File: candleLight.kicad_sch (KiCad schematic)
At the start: 3 parts

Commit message: schematic
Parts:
- removed FID101, FID102, FID103: Dummy_FIDUCIAL_Passermarke_Type1_RevE_Date16Nov20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, Fiducials:Fiducial_1mm_Dia_2.54mm_Outer_CopperTop, symbol candleLight-rescue:Dummy_FIDUCIAL_Passermarke_Type1_RevE_Date16Nov2011
- added C1, C10, C2: 10uF, Capacitor_SMD:C_0805_2012Metric, symbol candleLight-rescue:C_Small
- added C11, C12, C5, C6, C7, C8, C9: 100nF, Capacitor_SMD:C_0603_1608Metric, symbol candleLight-rescue:C_Small
- added C3, C4: 20pF, Capacitor_SMD:C_0603_1608Metric, symbol candleLight-rescue:C_Small
- added D1, D2, D3: LED, LED_SMD:LED_0603_1608Metric, symbol candleLight-rescue:LED
- added J1: USB_C_Receptacle_USB2.0, stm32world:USB_C_Receptacle_HRO_TYPE-C-31-M-12, symbol stm32world:USB_C_Receptacle_USB2.0
- added R1, R2: 4K7, Resistor_SMD:R_0603_1608Metric, symbol candleLight-rescue:R
- added R10, R4, R8, R9: 1K, Resistor_SMD:R_0603_1608Metric, symbol candleLight-rescue:R
- added R11, R5: 5k1, Resistor_SMD:R_0603_1608Metric, symbol Device:R
- added R3: R, Resistor_SMD:R_0805_2012Metric, symbol candleLight-rescue:R
- added R6: 10K, Resistor_SMD:R_0603_1608Metric, symbol candleLight-rescue:R
- added R7: dnp, Resistor_SMD:R_0805_2012Metric, symbol candleLight-rescue:R
- added SCL1: SCL1, Measurement_Points:Measurement_Point_Round-SMD-Pad_Small, symbol candleLight-rescue:TEST_1P
- added SDA1: SDA1, Measurement_Points:Measurement_Point_Round-SMD-Pad_Small, symbol candleLight-rescue:TEST_1P
- added U1: ME6210A33PG, Package_TO_SOT_SMD:SOT-89-3, symbol candleLight-rescue:MCP1754ST-3302E/MB
- added U2: STM32F072C8Tx, Package_QFP:LQFP-48_7x7mm_P0.5mm, symbol MCU_ST_STM32F0:STM32F072C8Tx
- added U3: TJA1051/3, Package_SO:SOIC-8_3.9x4.9mm_P1.27mm, symbol candleLight-rescue:TJA1051/3
- added W1, W2: TEST_1P, Measurement_Points:Measurement_Point_Round-SMD-Pad_Big, symbol candleLight-rescue:TEST_1P
- added W3, W4, W5, W6, W7, W8: TEST_1P, Measurement_Points:Measurement_Point_Round-SMD-Pad_Small, symbol candleLight-rescue:TEST_1P
- added X1: CON_SWD, Connector:Tag-Connect_TC2030-IDC-NL_2x03_P1.27mm_Vertical, symbol Connector:Conn_ARM_SWD_TagConnect_TC2030-NL
- added X2: SUB-D9, Connect:DB9M_CI, symbol candleLight-rescue:SUB-D9
- added Y1: 8MHz, Crystal:Crystal_SMD_Abracon_ABM3-2Pin_5.0x3.2mm, symbol candleLight-rescue:Crystal_Small
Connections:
- new net: D1.2 (A), R8.1
- new net: R1.2, SCL1.1, U2.42 (PB6)
- new net: J1.A5 (CC1), R5.2
- new net: J1.B5 (CC2), R11.1
- new net: U2.27 (PB14), W5.1
- new net: R2.1, SDA1.1, U2.43 (PB7)
- new net: U2.25 (PB12), W3.1
- new net: R3.2, R4.2, U2.44 (BOOT0)
- new net: U2.30 (PA9), W7.1
- new net: D3.2 (A), R10.1
- new net: U2.26 (PB13), W4.1
- new net: C3.2, U2.5 (PF0), Y1.1
- new net: C4.2, U2.6 (PF1), Y1.2
- new net: U2.28 (PB15), W6.1
- new net: U2.31 (PA10), W8.1
- new net: D2.2 (A), R9.1
- new net +3V3: C10.1, C12.1, C2.1, C6.1, C7.1, C8.1, C9.1, R1.1, R10.2, R2.2, R3.1, R6.1, R8.2, R9.2, U1.3 (VO), U2.1 (VBAT), U2.24 (VDD), U2.36 (VDDIO2), U2.48 (VDD), U2.9 (VDDA), U3.5 (VIO), X1.1 (VCC)
- new net +5V: C1.1, C11.1, J1.A4 (VBUS), J1.A9 (VBUS), J1.B4 (VBUS), J1.B9 (VBUS), U1.2 (VI), U3.3 (VCC), W1.1
- new net CAN_H: R7.1, U3.7 (CAN_H), X2.7
- new net CAN_L: R7.2, U3.6 (CAN_L), X2.2
- new net CAN_RX: U2.45 (PB8), U3.4 (RXD)
- new net CAN_S: R6.2, U2.2 (PC13), U3.8 (S)
- new net CAN_TX: U2.46 (PB9), U3.1 (TXD)
- new net GND: C1.2, C10.2, C11.2, C12.2, C2.2, C3.1, C4.1, C5.2, C6.2, C7.2, C8.2, C9.2, D3.1 (K), J1.A1 (GND), J1.A12 (GND), J1.B1 (GND), J1.B12 (GND), J1.S1 (SHIELD), R11.2, R4.1, R5.1, U1.1 (GND), U2.23 (VSS), U2.35 (VSS), U2.47 (VSS), U2.8 (VSSA), U3.2 (GND), W2.1, X1.3 (GND), X2.3
- new net LED1: D1.1 (K), U2.10 (PA0)
- new net LED2: D2.1 (K), U2.11 (PA1)
- new net NRST: C5.1, U2.7 (NRST), X1.5 (~{RESET})
- new net SWCLK: U2.37 (PA14), X1.2 (SWCLK)
- new net SWDIO: U2.34 (PA13), X1.4 (SWDIO)
- new net USB_DN: J1.A7 (D-), J1.B7 (D-), U2.32 (PA11)
- new net USB_DP: J1.A6 (D+), J1.B6 (D+), U2.33 (PA12)
- no-connect marks 0 -> 28
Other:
- removed sheet CAN
- removed sheet Connectors
- removed sheet LEDs
- removed sheet MCU
- removed sheet Power
- note added: "CAN"
- note added: "Connectors"
- note added: "Leds"
- note added: "MCU"
- note added: "Power"
- title: (none) -> canleLight

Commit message: v2 ready
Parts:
- removed X1: CON_SWD, Connector:Tag-Connect_TC2030-IDC-NL_2x03_P1.27mm_Vertical, symbol Connector:Conn_ARM_SWD_TagConnect_TC2030-NL
- removed X2: SUB-D9, Connect:DB9M_CI, symbol candleLight-rescue:SUB-D9
- added J2: Conn_Phoenix, TerminalBlock_Phoenix:TerminalBlock_Phoenix_MKDS-1,5-3-5.08_1x03_P5.08mm_Horizontal, symbol Connector_Generic:Conn_01x03
- added J3: Conn_SWD, Connector_PinHeader_2.54mm:PinHeader_1x03_P2.54mm_Vertical, symbol Connector_Generic:Conn_01x03
- added J4: Conn_3.3V, Connector_PinHeader_2.54mm:PinHeader_1x02_P2.54mm_Vertical, symbol Connector_Generic:Conn_01x02
- C3, C4: MPN C91702 -> C1648
- C5: MPN C105621 -> C14663
- R11, R5: MPN (none) -> C23186
- U3: symbol candleLight-rescue:TJA1051/3 -> Interface_CAN_LIN:TJA1051T-3; MPN C51484082 -> C58988
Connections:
- net +3V3: now also J4.1 (Pin_1)
- net CAN_H: now also J2.3 (Pin_3)
- net CAN_L: now also J2.1 (Pin_1)
- net GND: now also J2.2 (Pin_2), J4.2 (Pin_2)
- net NRST: now also J3.1 (Pin_1)
- net SWCLK: now also J3.2 (Pin_2)
- net SWDIO: now also J3.3 (Pin_3)
- no-connect marks 28 -> 20
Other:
- moved on the sheet: C1, C10, C11, C12, C2, C3, C4, C5, C6, C7, C8, C9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

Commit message: production :)
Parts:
- C3, C4: value 20pF -> 30pF; MPN C1648 -> C1658
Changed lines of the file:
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@@
 			)
 		)
-		(property "Value" "20pF"
+		(property "Value" "30pF"
 			(at 65.786 51.816 90)
 			(effects
@@
 			)
 		)
-		(property "MPN" "C1648"
+		(property "MPN" "C1658"
 			(at 63.5 54.61 90)
 			(effects
@@
 		(dnp no)
 		(property "Reference" "C4"
-			(at 62.23 61.214 90)
+			(at 62.23 60.706 90)
 			(effects
 				(font
@@
 			)
 		)
-		(property "Value" "20pF"
+		(property "Value" "30pF"
 			(at 66.294 62.484 90)
 			(effects
@@
 			)
 		)
-		(property "MPN" "C1648"
+		(property "MPN" "C1658"
 			(at 63.5 59.69 90)
 			(effects

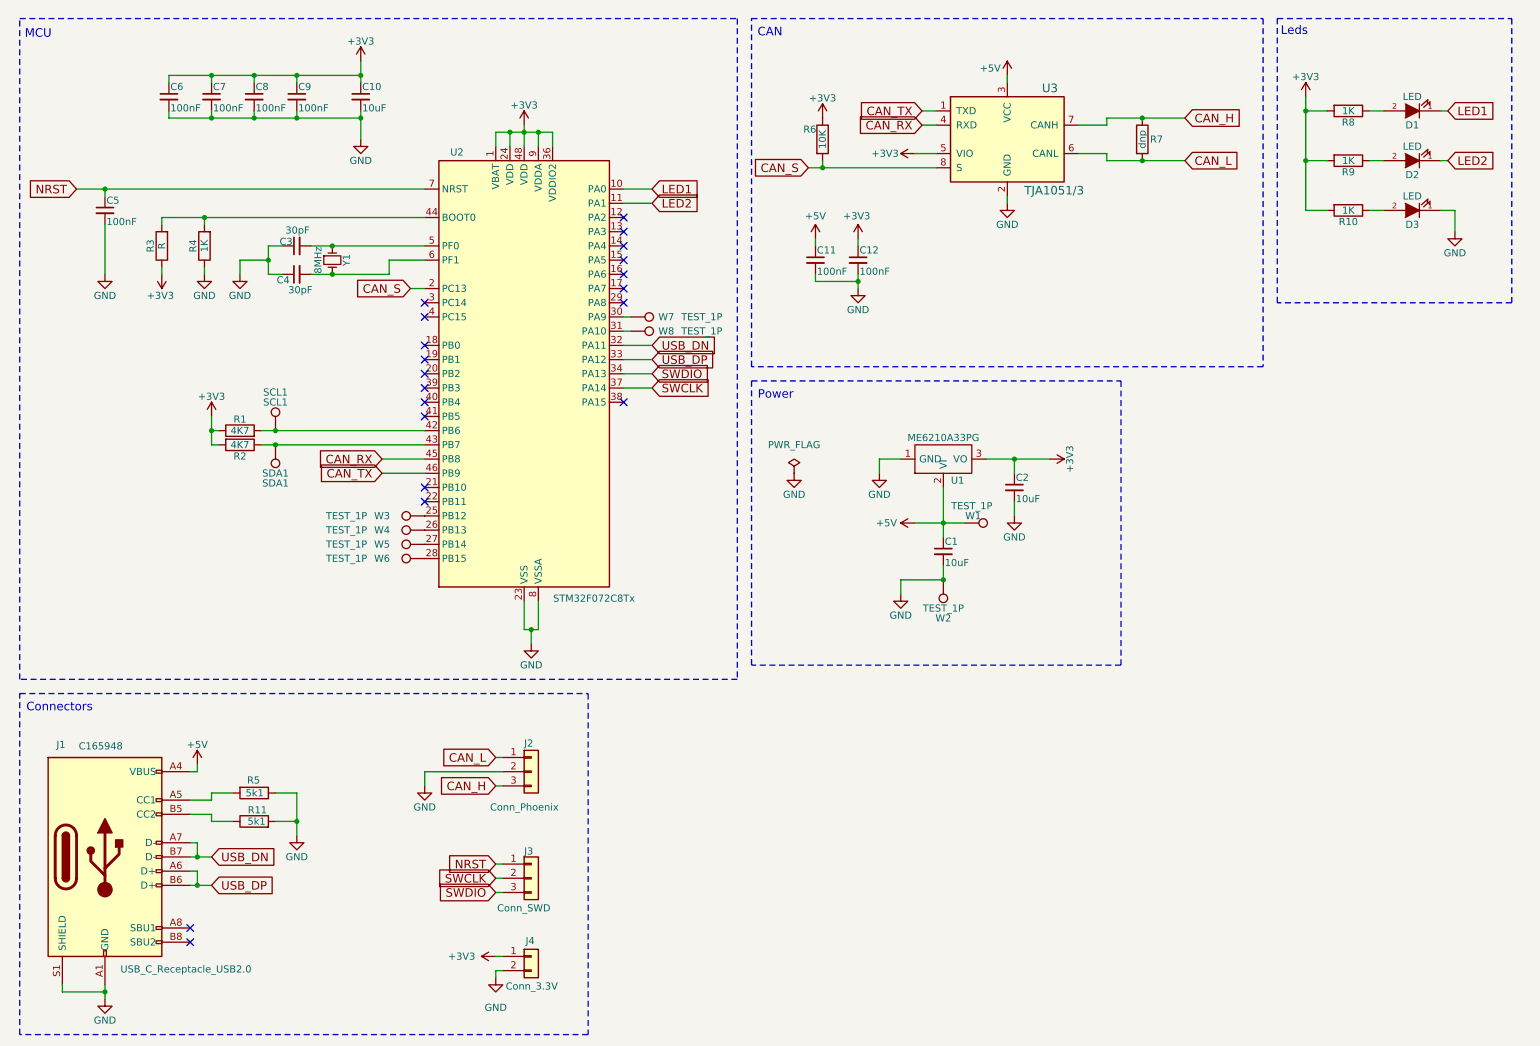
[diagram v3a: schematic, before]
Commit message: update schematic
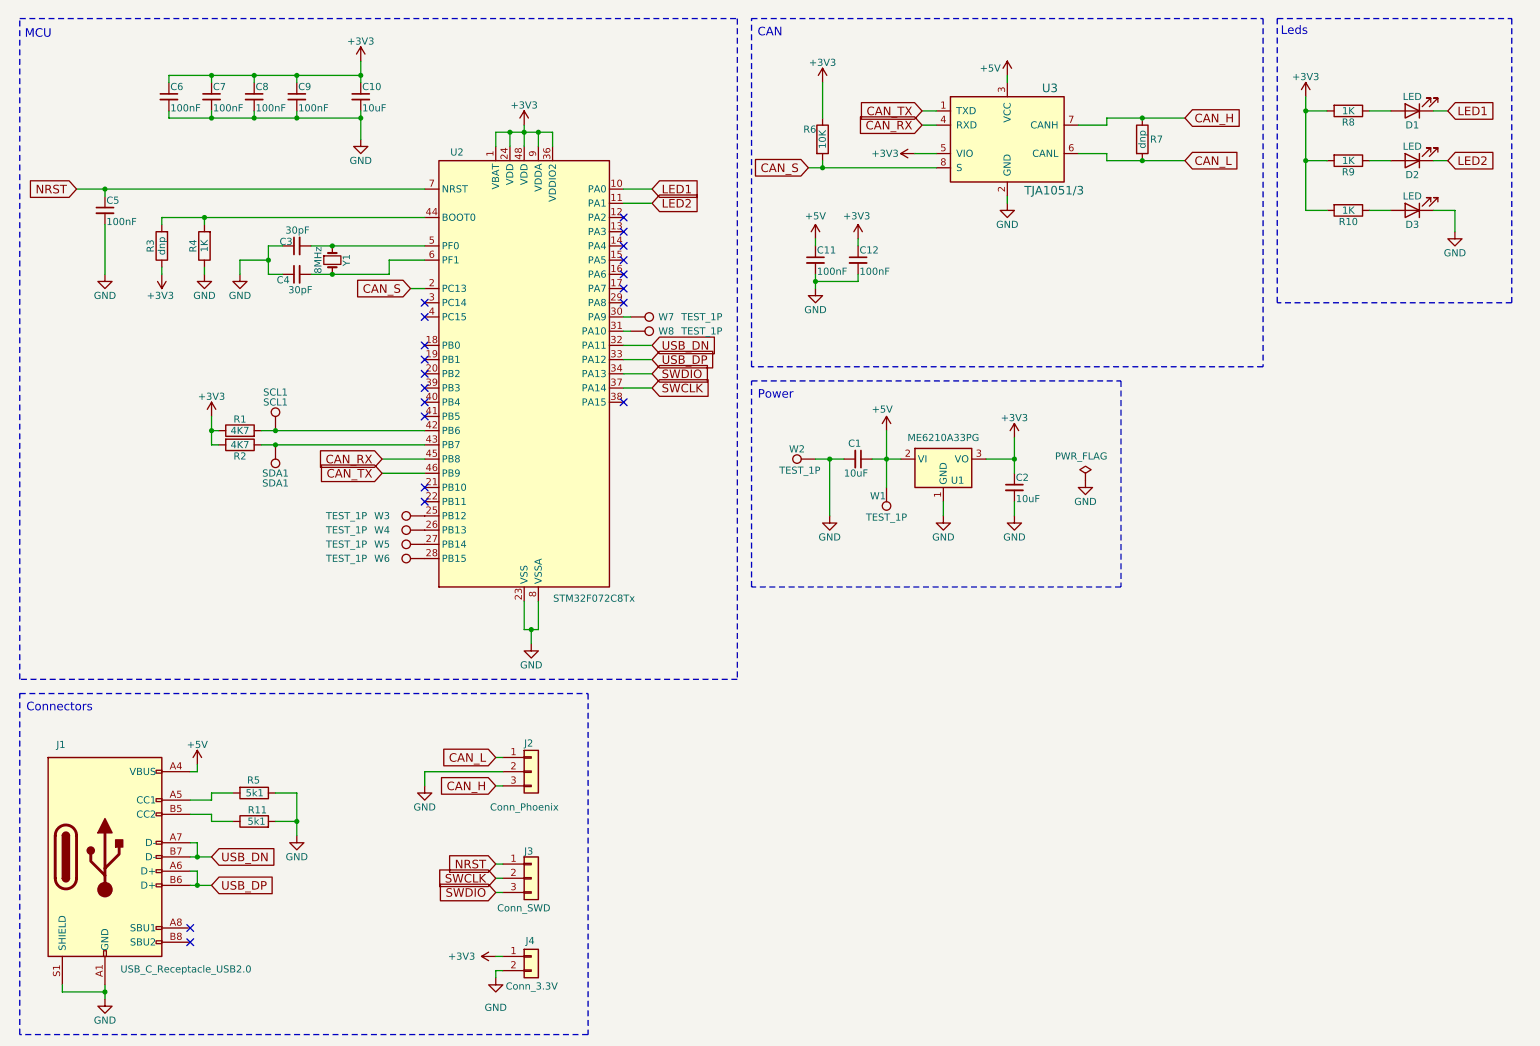
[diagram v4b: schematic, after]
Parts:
- C1, C10, C11, C12, C2, C3, C4, C5, C6, C7, C8, C9: symbol candleLight-rescue:C_Small -> Device:C_Small
- D1, D2, D3: symbol candleLight-rescue:LED -> Device:LED
- R1, R10, R2, R4, R6, R7, R8, R9: symbol candleLight-rescue:R -> Device:R
- R3: value R -> dnp; symbol candleLight-rescue:R -> Device:R
- SCL1, SDA1, W1, W2, W3, W4, W5, W6, W7, W8: symbol candleLight-rescue:TEST_1P -> Connector:TestPoint
- U1: symbol candleLight-rescue:MCP1754ST-3302E/MB -> Regulator_Linear:MCP1754S-1802xMB
- Y1: symbol candleLight-rescue:Crystal_Small -> Device:Crystal_Small
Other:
- moved on the sheet: C1, W1, W2

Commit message: LCSC
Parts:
- C1, C10, C2: LCSC (none) -> C440198; MPN C440198 -> (none)
- C11, C12, C5, C6, C7, C8, C9: LCSC (none) -> C14663; MPN C14663 -> (none)
- C3, C4: LCSC (none) -> C1658; MPN C1658 -> (none)
- D1, D2: LCSC (none) -> C2290; MPN C2290 -> (none)
- D3: LCSC (none) -> C2286; MPN C2286 -> (none)
- R1, R2: LCSC (none) -> C23162; MPN C23162 -> (none)
- R10, R4, R8, R9: LCSC (none) -> C21190; MPN C21190 -> (none)
- R11, R5: LCSC (none) -> C23186; MPN C23186 -> (none)
- R6: LCSC (none) -> C25804; MPN C25804 -> (none)
- U1: LCSC (none) -> C85233; MPN C85233 -> (none)
- U2: LCSC (none) -> C80488; MPN C80488 -> (none)
- U3: LCSC (none) -> C58988; MPN C58988 -> (none)
- Y1: LCSC (none) -> C144380; MPN C144380 -> (none)
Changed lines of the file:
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@@
 			)
 		)
-		(property "MPN" "C2290"
+		(property "LCSC" "C2290"
 			(at 262.89 30.48 0)
 			(effects
@@
 			)
 		)
-		(property "MPN" "C25804"
+		(property "LCSC" "C25804"
 			(at 157.48 35.56 90)
 			(effects
@@
 			)
 		)
-		(property "MPN" "C14663"
+		(property "LCSC" "C14663"
 			(at 55.88 27.94 0)
 			(effects
@@
 			)
 		)
-		(property "MPN" "C440198"
+		(property "LCSC" "C440198"
 			(at 191.77 97.79 0)
 			(effects
@@
 			)
 		)
-		(property "MPN" "C21190"
+		(property "LCSC" "C21190"
 			(at 251.46 30.48 90)
 			(effects
@@
 			)
 		)
-		(property "MPN" "C14663"
+		(property "LCSC" "C14663"
 			(at 48.26 27.94 0)
 			(effects
@@
 			)
 		)
-		(property "MPN" "C23162"
+		(property "LCSC" "C23162"
 			(at 53.34 90.17 90)
 			(effects
@@
 			)
 		)
-		(property "MPN" "C14663"
+		(property "LCSC" "C14663"
 			(at 163.83 57.15 0)
 			(effects
@@
 			)
 		)
-		(property "MPN" "C14663"
+		(property "LCSC" "C14663"
 			(at 156.21 57.15 0)
 			(effects
@@
 			)
 		)
-		(property "MPN" "C23186"
+		(property "LCSC" "C23186"
 			(at 55.88 157.48 90)
 			(effects
@@
 			)
 		)
-		(property "MPN" "C2286"
+		(property "LCSC" "C2286"
 			(at 262.89 48.26 0)
 			(effects
@@
 			)
 		)
-		(property "MPN" "C1658"
+		(property "LCSC" "C1658"
 			(at 63.5 54.61 90)
 			(effects
@@
 			)
 		)
-		(property "MPN" "C1658"
+		(property "LCSC" "C1658"
 			(at 63.5 59.69 90)
 			(effects
@@
 			)
 		)
-		(property "MPN" "C80488"
+		(property "LCSC" "C80488"
 			(at 104.14 77.47 0)
 			(effects
@@
 			)
 		)
-		(property "MPN" "C21190"
+		(property "LCSC" "C21190"
 			(at 46.99 54.61 90)
 			(effects
@@
 			)
 		)
-		(property "MPN" "C2290"
+		(property "LCSC" "C2290"
 			(at 262.89 39.37 0)
 			(effects
@@
 			)
 		)
-		(property "MPN" "C23186"
+		(property "LCSC" "C23186"
 			(at 55.88 152.4 90)
 			(effects
@@
 			)
 		)
-		(property "MPN" "C58988"
+		(property "LCSC" "C58988"
 			(at 190.5 35.56 0)
 			(effects
@@
 			)
 		)
-		(property "MPN" "C440198 "
+		(property "LCSC" "C440198 "
 			(at 74.93 27.94 0)
 			(effects
@@
 			)
 		)
-		(property "MPN" "C14663"
+		(property "LCSC" "C14663"
 			(at 63.5 27.94 0)
 			(effects
@@
 			)
 		)
-		(property "MPN" "C21190"
+		(property "LCSC" "C21190"
 			(at 251.46 39.37 90)
 			(effects
@@
 			)
 		)
-		(property "MPN" "C14663"
+		(property "LCSC" "C14663"
 			(at 40.64 27.94 0)
 			(effects
@@
 			)
 		)
-		(property "MPN" "C144380"
+		(property "LCSC" "C144380"
 			(at 69.85 57.15 0)
 			(effects
@@
 			)
 		)
-		(property "MPN" "C21190"
+		(property "LCSC" "C21190"
 			(at 251.46 48.26 90)
 			(effects
@@
 			)
 		)
-		(property "MPN" "C85233"
+		(property "LCSC" "C85233"
 			(at 179.07 92.71 0)
 			(effects
@@
 			)
 		)
-		(property "MPN" "C440198"
+		(property "LCSC" "C440198"
 			(at 163.83 92.71 0)
 			(effects
@@
 			)
 		)
-		(property "MPN" "C23162"
+		(property "LCSC" "C23162"
 			(at 53.34 87.63 90)
 			(effects
@@
 			)
 		)
-		(property "MPN" "C14663"
+		(property "LCSC" "C14663"
 			(at 29.21 48.26 0)
 			(effects

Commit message: inital board
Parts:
- removed C5: 100nF, Capacitor_SMD:C_0603_1608Metric, symbol Device:C_Small
- removed J3: Conn_SWD, Connector_PinHeader_2.54mm:PinHeader_1x03_P2.54mm_Vertical, symbol Connector_Generic:Conn_01x03
- removed J4: Conn_3.3V, Connector_PinHeader_2.54mm:PinHeader_1x02_P2.54mm_Vertical, symbol Connector_Generic:Conn_01x02
- removed R1, R2: 4K7, Resistor_SMD:R_0603_1608Metric, symbol Device:R
- removed R3: dnp, Resistor_SMD:R_0805_2012Metric, symbol Device:R
- removed R4: 1K, Resistor_SMD:R_0603_1608Metric, symbol Device:R
- removed SCL1: SCL1, Measurement_Points:Measurement_Point_Round-SMD-Pad_Small, symbol Connector:TestPoint
- removed SDA1: SDA1, Measurement_Points:Measurement_Point_Round-SMD-Pad_Small, symbol Connector:TestPoint
- removed W1, W2: TEST_1P, Measurement_Points:Measurement_Point_Round-SMD-Pad_Big, symbol Connector:TestPoint
- removed W3, W4, W5, W6, W7, W8: TEST_1P, Measurement_Points:Measurement_Point_Round-SMD-Pad_Small, symbol Connector:TestPoint
- added C13, C14, C3: 100nF, Capacitor_SMD:C_0603_1608Metric, symbol Device:C_Small
- added C15: 10uF, Capacitor_SMD:C_0805_2012Metric, symbol Device:C_Small
- added J3: Conn_01x05, Connector_PinHeader_2.54mm:PinHeader_1x05_P2.54mm_Vertical, symbol Connector_Generic:Conn_01x05
- added R5: 10K, Resistor_SMD:R_0603_1608Metric, symbol Device:R
- added R8: 120, Resistor_SMD:R_0603_1608Metric, symbol Device:R
- added SW1, SW2: TS-1088R-02526, stm32world:TS-1088R-02526, symbol stm32world:TS-1088R-02526
- added SW3: MST22D18G2 125, woldhack:SW-SMD_MST22D18G2, symbol woldhack:MST22D18G2125
- C1: renamed from C3; LCSC C1658 -> C1554
- C12: renamed from C10; LCSC C440198 -> C440198
- C2: renamed from C4; LCSC C1658 -> C1554
- R7: value dnp -> 10K; footprint Resistor_SMD:R_0805_2012Metric -> Resistor_SMD:R_0603_1608Metric; LCSC (none) -> C25804
- Y1: LCSC C144380 -> C115962
- renumbered C8 to C10, C9 to C11, C1 to C4, C2 to C5, C11 to C6, C6 to C7, C12 to C8, C7 to C9, R9 to R10, R10 to R11, R5 to R3, R11 to R4, R8 to R9, U2 to U1, U1 to U2
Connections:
- net +3V3: now also C13.1, C14.1, C15.1, J3.1 (Pin_1), R5.1, SW2.2
- net CAN_H: now also SW3.5; no longer R7.1
- net CAN_L: now also R8.2; no longer R7.2
- net GND: now also R7.2, C13.2, C14.2, C15.2, C3.2, J3.5 (Pin_5), SW1.1
- net NRST: now also C3.1, J3.2 (Pin_2), R5.2, SW1.2
- net SWCLK: now also J3.3 (Pin_3)
- net SWDIO: now also J3.4 (Pin_4)
- net BO0: now reaches U1.44 (BOOT0)
- net BO0: now also R7.1, SW2.1
- new net: R8.1, SW3.6
- no-connect marks 20 -> 32
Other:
- note added: "Decoupling"
- note added: "Reset and boot0"
- note added: "VBAT"
- note added: "VDA"
- note added: "VDD"
- note added: "VDDIO2"
- moved on the sheet: C1, C10, C11, C12, C2, C4, C5, C6, C7, C8, C9, D1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

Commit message: layout
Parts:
- removed C11: 100nF, Capacitor_SMD:C_0603_1608Metric, symbol Device:C_Small
- removed C4, C5: 10uF, Capacitor_SMD:C_0805_2012Metric, symbol Device:C_Small
- removed SW1, SW2: TS-1088R-02526, stm32world:TS-1088R-02526, symbol stm32world:TS-1088R-02526
- removed U2: ME6210A33PG, Package_TO_SOT_SMD:SOT-89-3, symbol Regulator_Linear:MCP1754S-1802xMB
- removed U3: TJA1051/3, Package_SO:SOIC-8_3.9x4.9mm_P1.27mm, symbol Interface_CAN_LIN:TJA1051T-3
- added C4, C5: C_10UF_0805, Capacitor_SMD:C_0805_2012Metric, symbol stm32world:C_10UF_0805
- added D4: PSM712, Package_TO_SOT_SMD:SOT-23, symbol Power_Protection:SP0502BAHT
- added D5: ~, Diode_SMD:D_SOD-123, symbol Device:D_Schottky
- added H1, H2, H3, H4: MountingHole, MountingHole:MountingHole_2.1mm, symbol Mechanical:MountingHole
- added J4: Conn_USART1, Connector_PinHeader_2.54mm:PinHeader_1x02_P2.54mm_Vertical, symbol Connector_Generic:Conn_01x02
- added J5: Conn_BOOT0, Connector_PinHeader_2.54mm:PinHeader_1x03_P2.54mm_Vertical, symbol Connector_Generic:Conn_01x03
- added U2: AMS1117-3.3, Package_TO_SOT_SMD:SOT-223-3_TabPin2, symbol stm32world:AMS1117-3.3
- added U3: TJA1051TK-3, Package_DFN_QFN:DFN-8-1EP_3x3mm_P0.65mm_EP1.55x2.4mm, symbol Interface_CAN_LIN:TJA1051TK-3
- C1, C2: value 30pF -> 20pF
- J3: value Conn_01x05 -> Conn_SWD
- renumbered C12 to C11, C13 to C12, C14 to C13, C15 to C14, R3 to R1, R4 to R2, R5 to R3, R6 to R4, R7 to R5, R8 to R6, R9 to R7, R10 to R8, R11 to R9, SW3 to SW1
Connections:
- net +3V3: now also C5.1, J5.1 (Pin_1), U2.2 (VO), U3.5 (VIO)
- net +5V: now also C4.1, D5.1 (K), U2.3 (VI), U3.3 (VCC); no longer J1.A4 (VBUS), J1.A9 (VBUS), J1.B4 (VBUS), J1.B9 (VBUS)
- net BO0: now also J5.2 (Pin_2); no longer U1.44 (BOOT0)
- net CAN_RX: now also U3.4 (RXD)
- net CAN_S: now also U3.8 (S)
- net CAN_TX: now also U3.1 (TXD)
- net GND: now also J2.3 (Pin_3), C4.2, C5.2, D4.3 (A), J5.3 (Pin_3), U2.1 (GND), U3.2 (GND), U3.9 (GND); no longer J2.2 (Pin_2), R5.2
- net USB_DN: now also D4.1 (K)
- net USB_DP: now also D4.2 (K)
- net USART1_TX: now reaches U1.30 (PA9)
- net USART1_TX: now also J4.1 (Pin_1)
- net USART1_RX: now reaches U1.31 (PA10)
- net USART1_RX: now also J4.2 (Pin_2)
- net CAN_H renamed CAN_DP
- net CAN_DP: now also J2.2 (Pin_2), U3.7 (CANH); no longer J2.3 (Pin_3)
- net CAN_L renamed CAN_DN
- net CAN_DN: now also U3.6 (CANL)
- new net: R5.2, U1.44 (BOOT0)
- new net VBUS: D5.2 (A), J1.A4 (VBUS), J1.A9 (VBUS), J1.B4 (VBUS), J1.B9 (VBUS)
- no-connect marks 32 -> 30
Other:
- note removed: "Reset and boot0"
- moved on the sheet: C1, C10, C11, C12, C13, C14, C2, C3, C6, C7, C8, C9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
